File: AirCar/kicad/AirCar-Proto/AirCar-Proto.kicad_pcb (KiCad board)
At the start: 2 copper layers, 76.2 x 55.9 mm, 22 parts, among them J1 Conn_01x05, J3 Conn_01x06, J4 PJ-102A, SW2 SW_SPDT, U1 Pico, U2 LDL212PU50R, U3 TXU0104BQAR

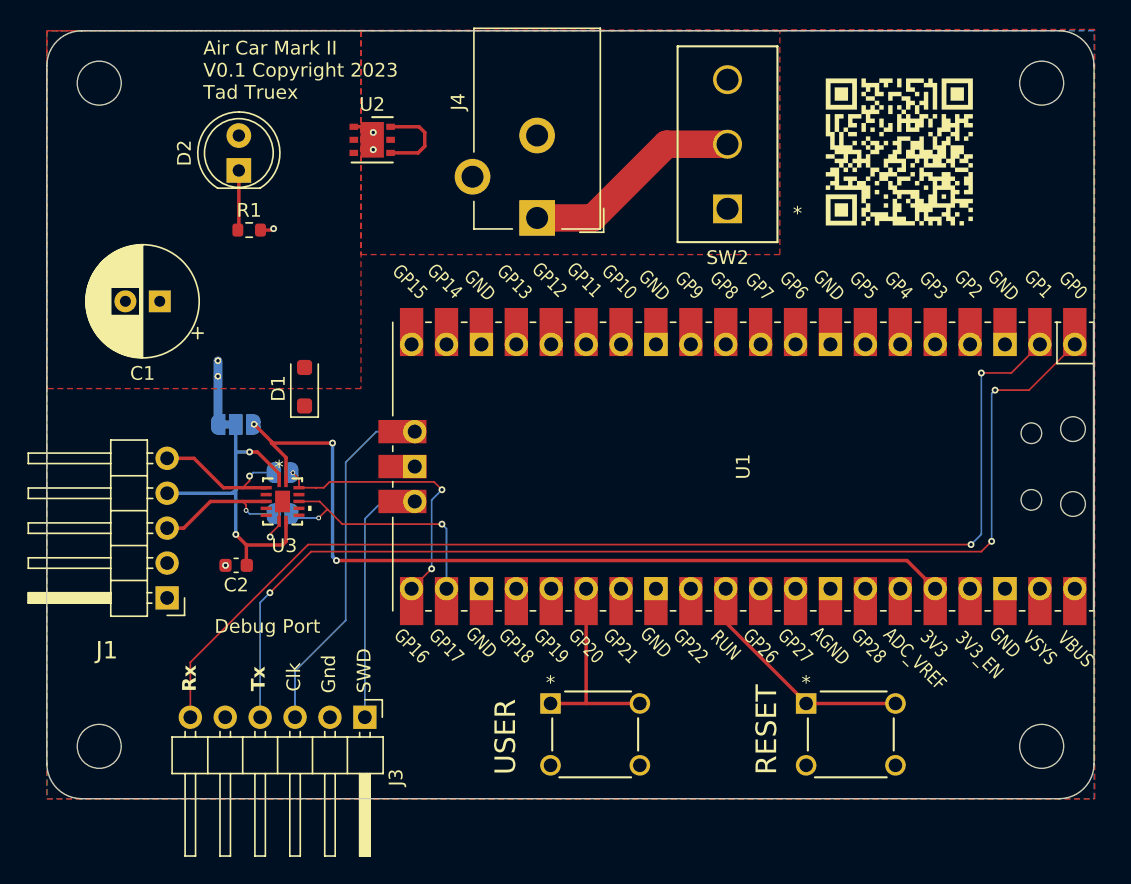
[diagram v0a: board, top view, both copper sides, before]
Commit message: remove small vias for JLCPCB
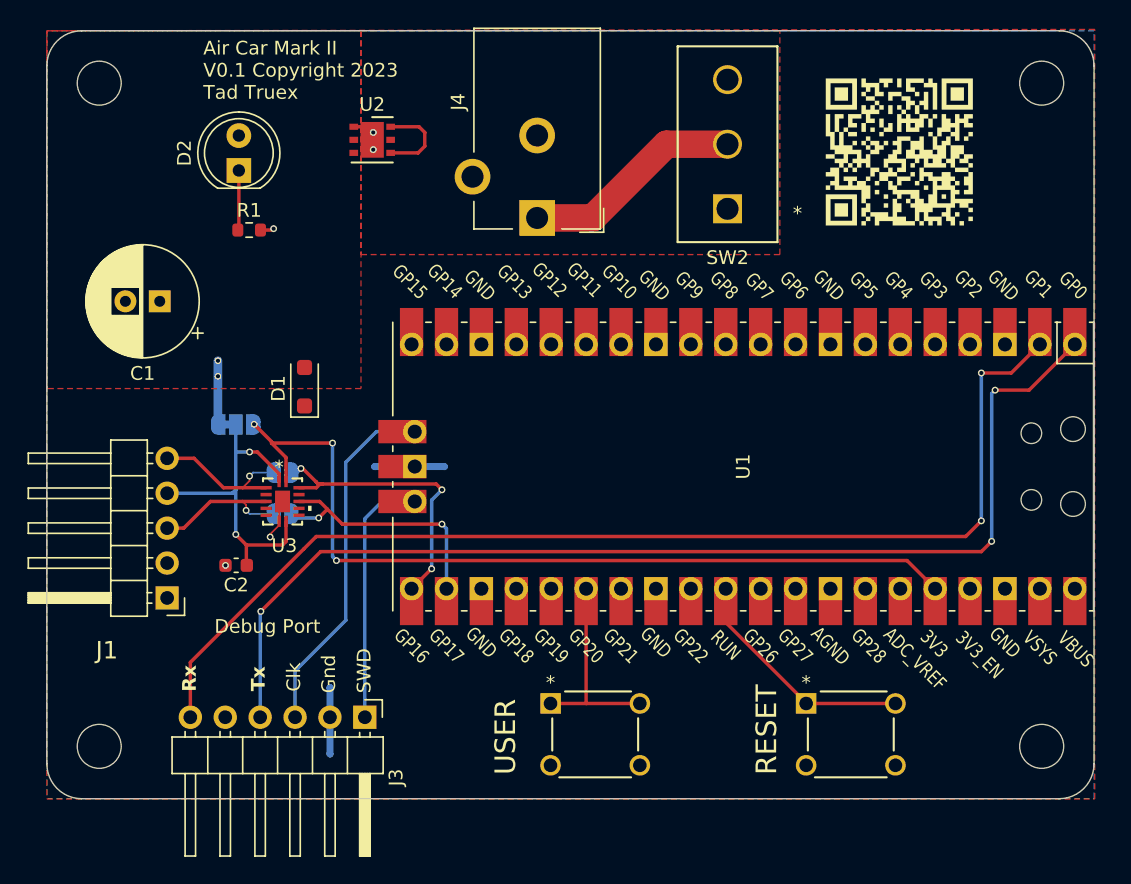
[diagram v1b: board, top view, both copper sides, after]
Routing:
- net GND: track 6.88 -> 16.8 mm
- net /Lag_3P3: track 20.2 -> 21.7 mm
- net /PicoRx: track 82.3 -> 81.7 mm
